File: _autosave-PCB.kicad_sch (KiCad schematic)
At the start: 12 parts, among them U1 ATmega32U4-A, Y1 16MHz

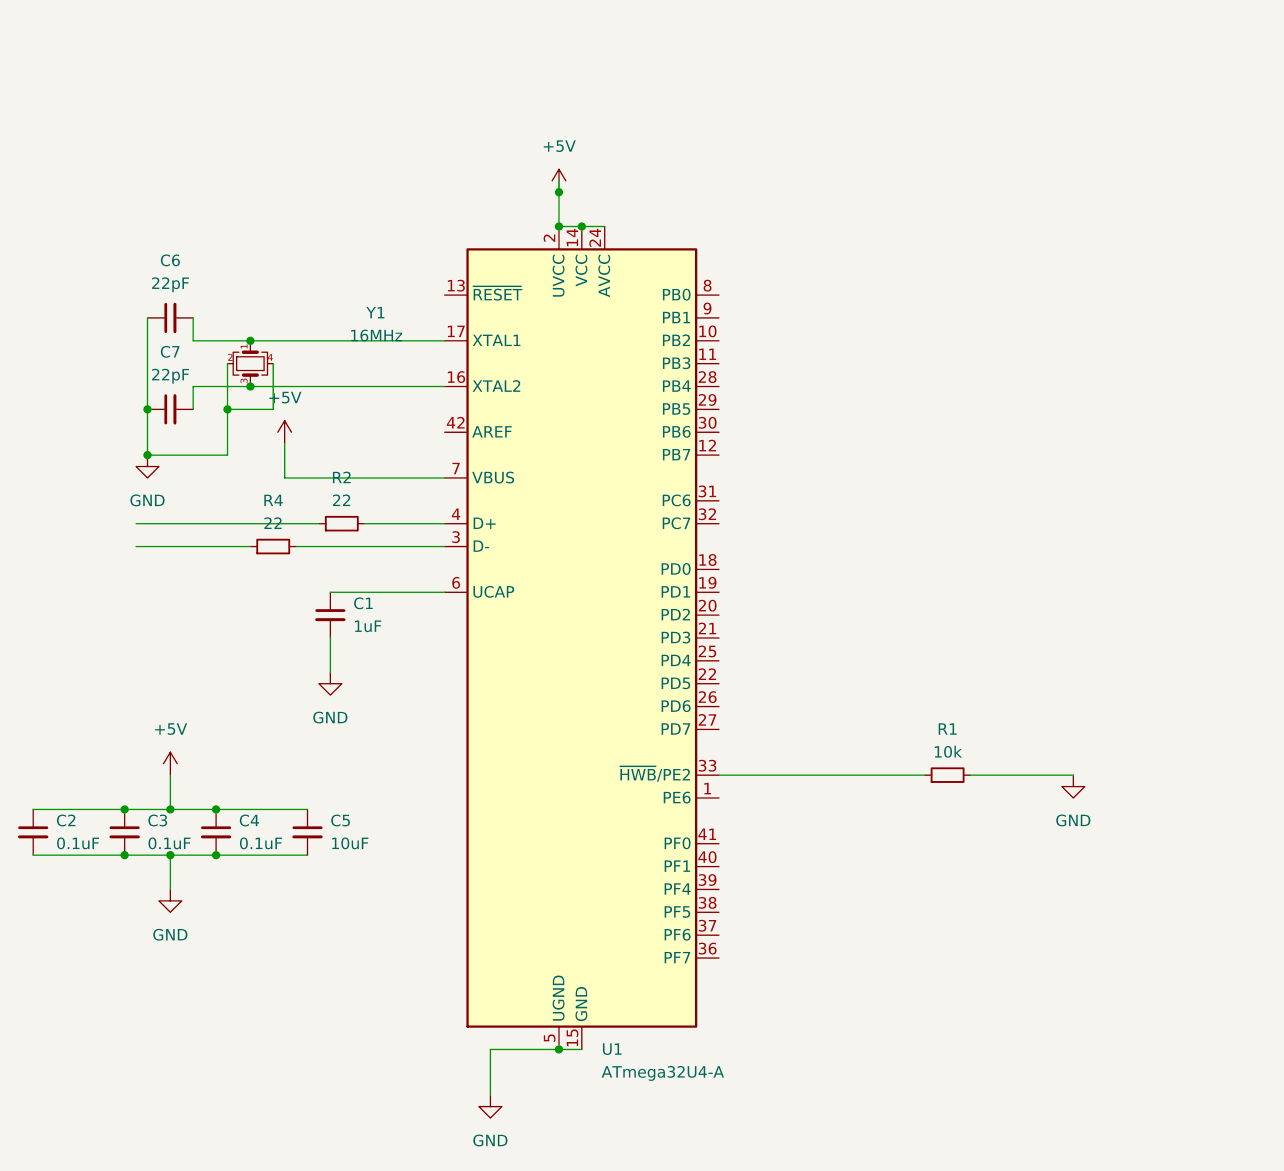
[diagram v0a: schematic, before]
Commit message: Add switches submodules
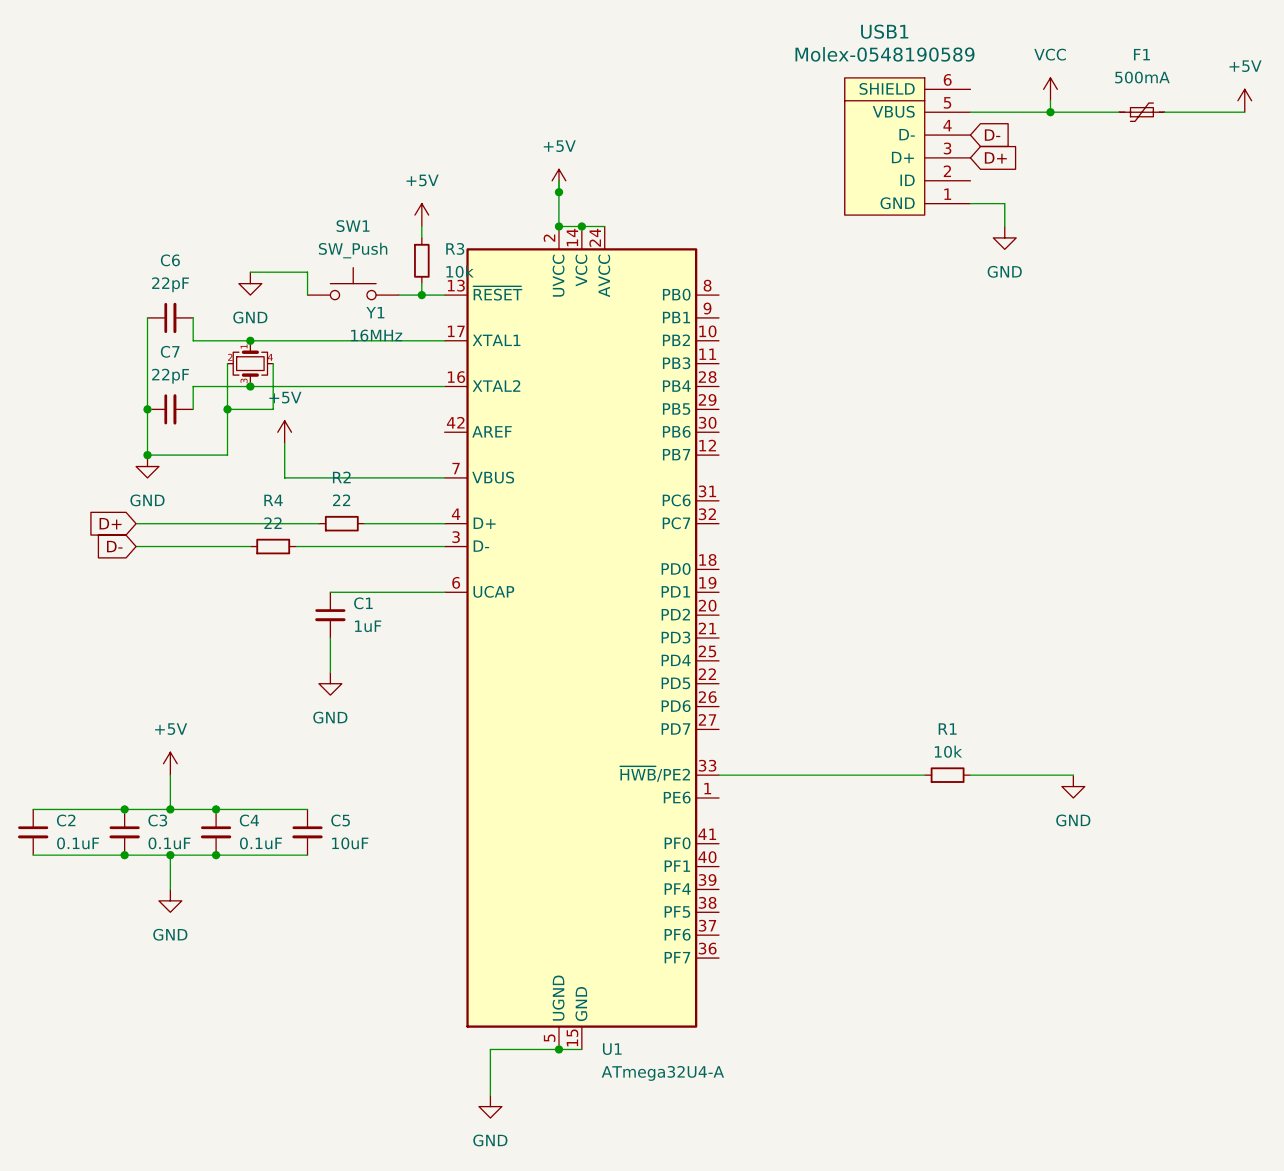
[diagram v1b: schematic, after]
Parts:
- added F1: 500mA, symbol Device:Polyfuse_Small
- added R3: 10k, symbol Device:R_Small
- added SW1: SW_Push, symbol Switch:SW_Push
- added USB1: Molex-0548190589, symbol random-keyboard-parts:Molex-0548190589
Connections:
- net +5V: now also F1.2, R3.1
- net GND: now also SW1.1, USB1.1 (GND)
- net at U1.13 (~{RESET}): now also R3.2, SW1.2
- net D-: now reaches R4.1
- net D-: now also USB1.4 (D-)
- net D+: now reaches R2.1
- net D+: now also USB1.3 (D+)
- new net VCC: F1.1, USB1.5 (VBUS)
